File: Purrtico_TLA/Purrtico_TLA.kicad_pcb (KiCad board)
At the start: 2 copper layers, 100 x 50 mm, 67 parts, among them J1 XLR3, J2 Conn_01x03, J3 Conn_01x02, J4 XLR3, J5 Conn_01x02, U1 OPA1679, U2 OPA1679

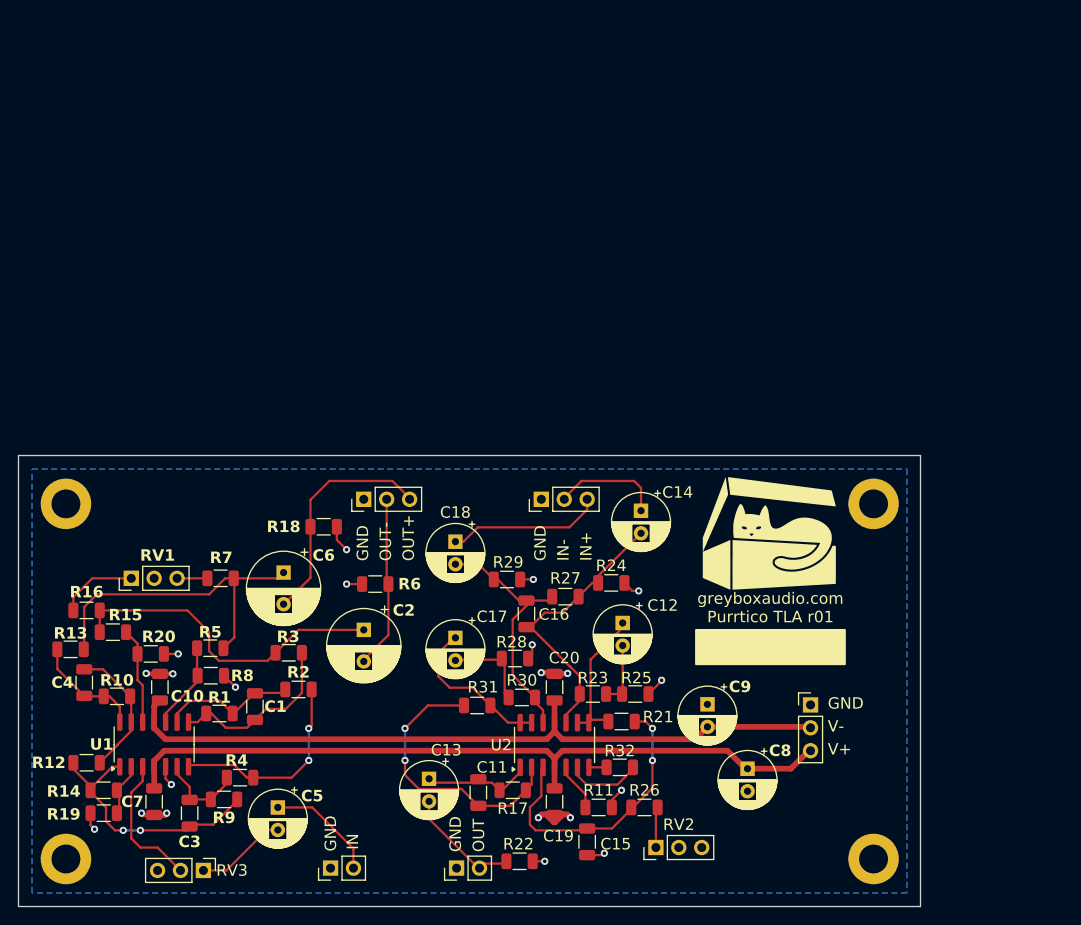
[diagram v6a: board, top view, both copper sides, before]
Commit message: update pcb
swapped position of input/output, replaced power connector with a 10pin eurorack connector
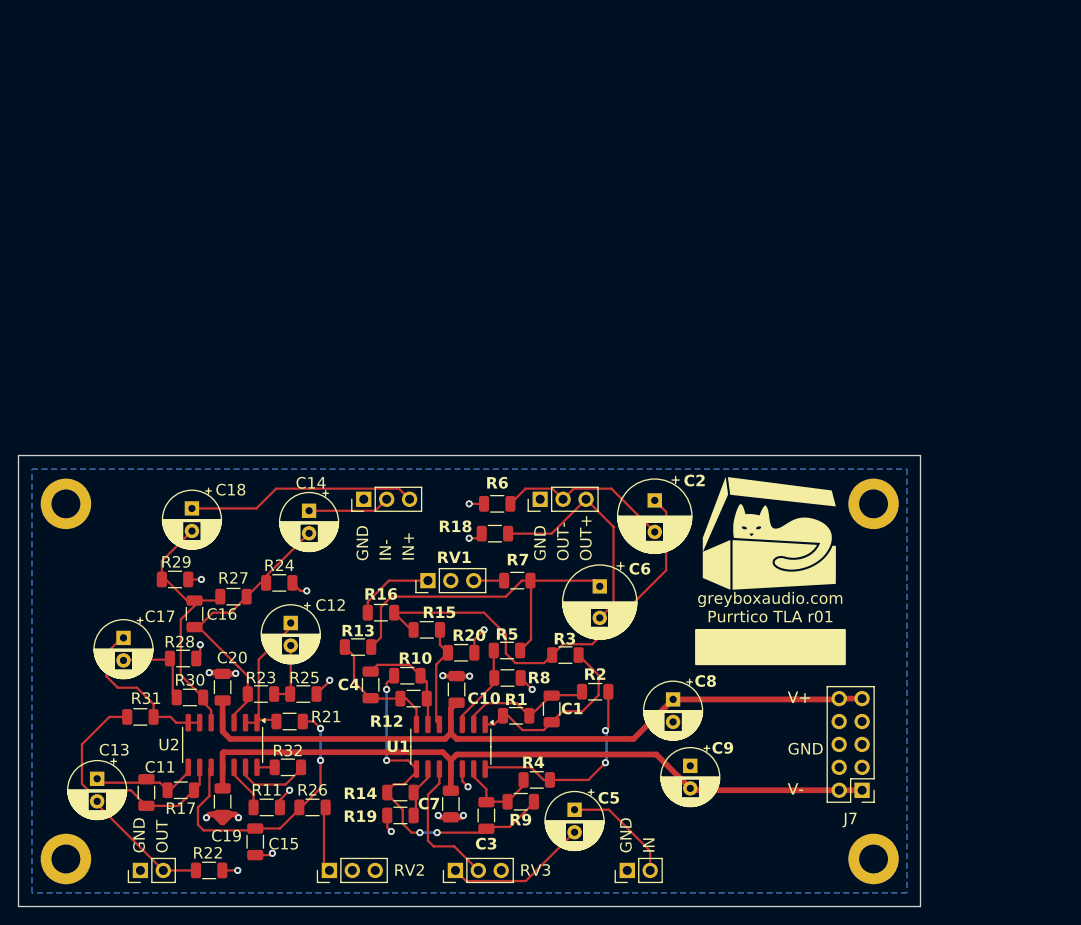
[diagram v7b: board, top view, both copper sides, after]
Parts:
- removed J2: Conn_01x03, Connector_PinHeader_2.54mm:PinHeader_1x03_P2.54mm_Vertical
- added J7: Conn_02x05_Odd_Even, Connector_PinHeader_2.54mm:PinHeader_2x05_P2.54mm_Vertical, F.Cu at (136.5, 118.1)
- moved R31 37.4 mm to (56.5, 110.0)
- moved R12 36.8 mm to (86.1, 105.4)
- moved R23 36.8 mm to (69.9, 107.4)
- moved C11 36.8 mm to (57.2, 118.4)
- moved C13 36.8 mm to (51.7, 116.8)
- moved R17 36.8 mm to (61.0, 118.1)
- moved C12 36.8 mm to (73.2, 99.6)
- moved C14 36.8 mm to (75.2, 87.1)
- moved C15 36.8 mm to (69.2, 123.8)
- moved C17 36.8 mm to (54.6, 101.2)
- moved C19 36.8 mm to (65.6, 119.4)
- moved C20 36.8 mm to (65.6, 106.7)
- moved R11 36.8 mm to (70.5, 120.0)
- moved R21 36.8 mm to (73.1, 110.5)
- moved R24 36.8 mm to (71.9, 95.1)
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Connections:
- C1 pad 1: Net-(U1C--) -> Net-(U1A--)
- C10 pad 2: -15V -> +15V
- C11 pad 2: Net-(U2A--) -> Net-(U2C--)
- C12 pad 1: Net-(U2C--) -> Net-(U2A--)
- C14 pad 2: Net-(U2C-+) -> Net-(U2A-+)
- C15 pad 1: Net-(U2A-+) -> Net-(U2C-+)
- C16 pad 1: Net-(U2D-+) -> Net-(U2B-+)
- C16 pad 2: Net-(U2C-+) -> Net-(U2A-+)
- C17 pad 1: Net-(U2D--) -> Net-(U2B--)
- C18 pad 2: Net-(U2D-+) -> Net-(U2B-+)
- C19 pad 1: +15V -> -15V
- C20 pad 2: -15V -> +15V
- C3 pad 2: Net-(U1B--) -> Net-(U1D--)
- C4 pad 1: Net-(U1D--) -> Net-(U1B--)
- C7 pad 1: +15V -> -15V
- R1 pad 1: Net-(U1C--) -> Net-(U1A--)
- R10 pad 1: Net-(U1D--) -> Net-(U1B--)
- R11 pad 1: Net-(U2B-+) -> Net-(U2D-+)
- R12 pad 2: Net-(U1D--) -> Net-(U1B--)
- R14 pad 1: Net-(U1A--) -> Net-(U1C--)
- R15 pad 1: Net-(U1D-+) -> Net-(U1B-+)
- R17 pad 2: Net-(U2A--) -> Net-(U2C--)
- R19 pad 2: Net-(U1A--) -> Net-(U1C--)
- R2 pad 2: Net-(U1C--) -> Net-(U1A--)
- R20 pad 2: Net-(U1D-+) -> Net-(U1B-+)
- R21 pad 1: Net-(U2A-+) -> Net-(U2C-+)
- R21 pad 2: Net-(U2C--) -> Net-(U2A--)
- R23 pad 2: Net-(U2C-+) -> Net-(U2A-+)
- R24 pad 2: Net-(U2C-+) -> Net-(U2A-+)
- R26 pad 2: Net-(U2A-+) -> Net-(U2C-+)
- R27 pad 1: Net-(U2D-+) -> Net-(U2B-+)
- R27 pad 2: Net-(U2C-+) -> Net-(U2A-+)
- R29 pad 1: Net-(U2D-+) -> Net-(U2B-+)
- R30 pad 1: Net-(U2D-+) -> Net-(U2B-+)
- R31 pad 1: Net-(U2A--) -> Net-(U2C--)
- R31 pad 2: Net-(U2D--) -> Net-(U2B--)
- R32 pad 2: Net-(U2B--) -> Net-(U2D--)
- R4 pad 1: Net-(U1B--) -> Net-(U1D--)
- R5 pad 1: Net-(U1C-+) -> Net-(U1A-+)
- R8 pad 2: Net-(U1C-+) -> Net-(U1A-+)
- R9 pad 2: Net-(U1B--) -> Net-(U1D--)
- RV3 pad 2: Net-(U1A-+) -> Net-(U1C-+)
- U1 pad 1: Net-(C3-Pad1) -> Net-(C1-Pad2)
- U1 pad 12: Net-(U1D-+) -> GND
- U1 pad 14: Net-(C4-Pad2) -> Net-(R2-Pad1)
- U1 pad 5: GND -> Net-(U1B-+)
- U1 pad 7: Net-(R2-Pad1) -> Net-(C4-Pad2)
- U1 pad 8: Net-(C1-Pad2) -> Net-(C3-Pad1)
- U2 pad 1: Net-(C11-Pad1) -> Net-(U2A--)
- U2 pad 14: Net-(U2D--) -> Net-(R32-Pad1)
- U2 pad 7: Net-(R32-Pad1) -> Net-(U2B--)
- U2 pad 8: Net-(U2C--) -> Net-(C11-Pad1)
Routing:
- net Net-(U2D-+): track 29.3 -> 4.51 mm
- net Net-(U2B-+): track 5.34 -> 28.8 mm
- net Net-(U2A--): track 31.1 -> 15.1 mm, vias 2 -> 0
- net Net-(C2-Pad1): track 36.7 -> 48.9 mm
- net Net-(U2C--): track 15.9 -> 27.6 mm
- net Net-(U1B-+): track 0.00 -> 11.5 mm
- net Net-(U1D-+): track 10.7 -> 0.00 mm
- net Net-(U1C--): track 15.2 -> 5.06 mm
- net Net-(U2B--): track 8.46 -> 18.3 mm
- net Net-(U1A--): track 5.06 -> 14.4 mm
- net Net-(U2D--): track 17.6 -> 8.46 mm
- net Net-(C18-Pad1): track 17.3 -> 25.5 mm
- net Net-(U1C-+): track 8.45 -> 15.4 mm
- net Net-(U1A-+): track 15.4 -> 8.45 mm
- net Net-(C3-Pad1): track 30.5 -> 37.3 mm, vias 2 -> 4
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
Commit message: update pcb
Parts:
- moved H3 51.6 mm to (64.8, 76.8)
- moved J1 51.6 mm to (116.9, 36.8)
- moved J4 51.5 mm to (97.2, 36.8)
- moved H4 51.2 mm to (153.0, 76.8)
- moved RV2 50.8 mm to (93.4, 78.7)
- moved RV3 50.8 mm to (107.3, 78.7)
- moved J3 50.8 mm to (126.4, 78.7)
- moved J5 50.8 mm to (72.4, 78.7)
- moved C11 50.8 mm to (73.2, 70.2)
- moved C13 50.8 mm to (67.7, 68.6)
- moved C15 50.8 mm to (85.2, 75.6)
- moved C16 50.8 mm to (78.5, 50.3)
- moved C20 50.8 mm to (81.6, 58.5)
- moved C5 50.8 mm to (120.6, 72.1)
- moved C6 50.8 mm to (123.4, 47.3)
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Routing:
- net Net-(C1-Pad2): track 20.6 -> 18.9 mm
- net Net-(U2A-+): track 29.9 -> 28.4 mm
- net Net-(C6-Pad2): track 25.3 -> 26.7 mm
- net Net-(U1A--): track 14.4 -> 13.0 mm
- net Net-(U2C--): track 27.6 -> 26.6 mm
- net Net-(C4-Pad2): track 14.0 -> 13.1 mm
- net Net-(U1B--): track 11.9 -> 10.9 mm
- net Net-(U2D--): track 8.46 -> 7.60 mm
- net Net-(U2B-+): track 28.8 -> 28.1 mm
- net GND: track 40.3 -> 39.6 mm
- net Net-(C2-Pad1): track 48.9 -> 49.6 mm
- net Net-(U2C-+): track 31.1 -> 30.4 mm
- net Net-(C3-Pad1): track 37.3 -> 36.6 mm
- net Net-(U1B-+): track 11.5 -> 10.9 mm
- net Net-(C6-Pad1): track 37.9 -> 37.3 mm
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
